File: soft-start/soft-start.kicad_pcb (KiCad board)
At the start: 2 copper layers, 26 parts, among them Q1 IRFB3004PbF, U1 4011, U2 CD4060BE

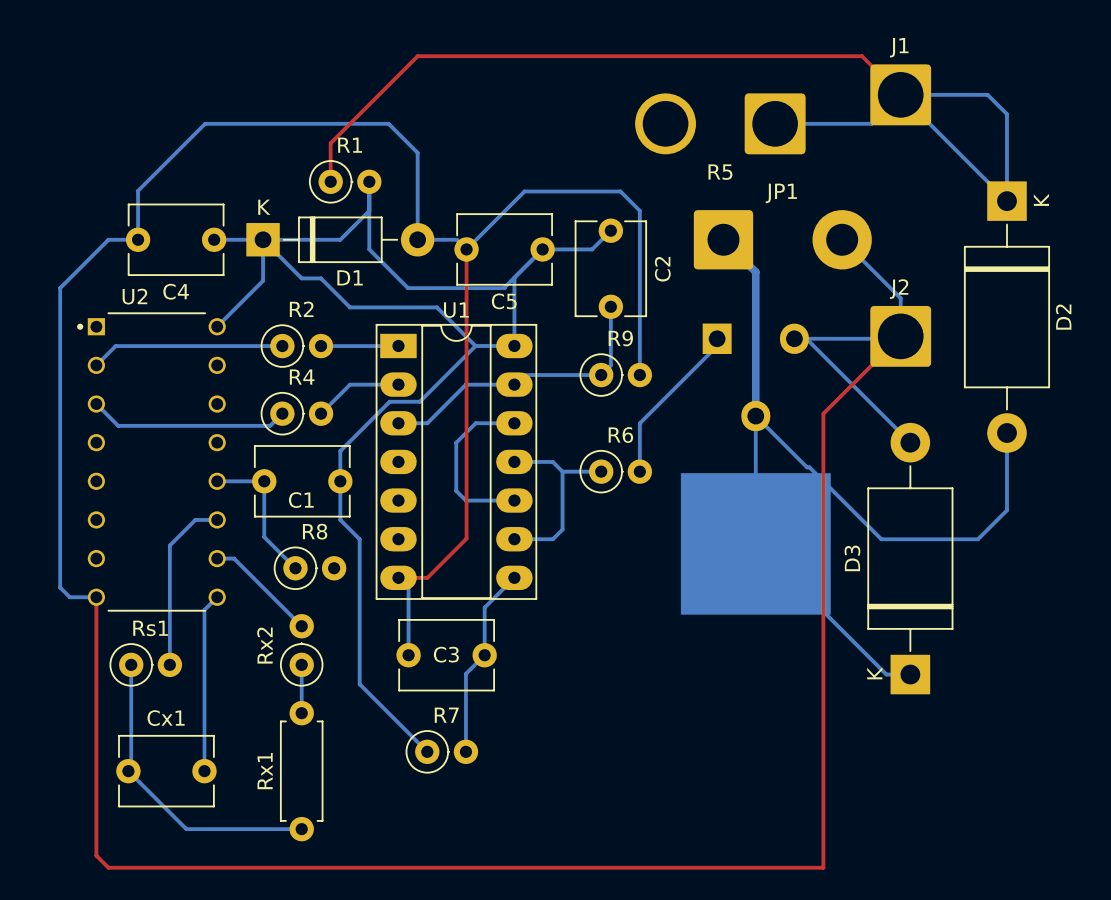
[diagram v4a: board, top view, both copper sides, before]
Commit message: [soft-start] Update schematic and add PCB
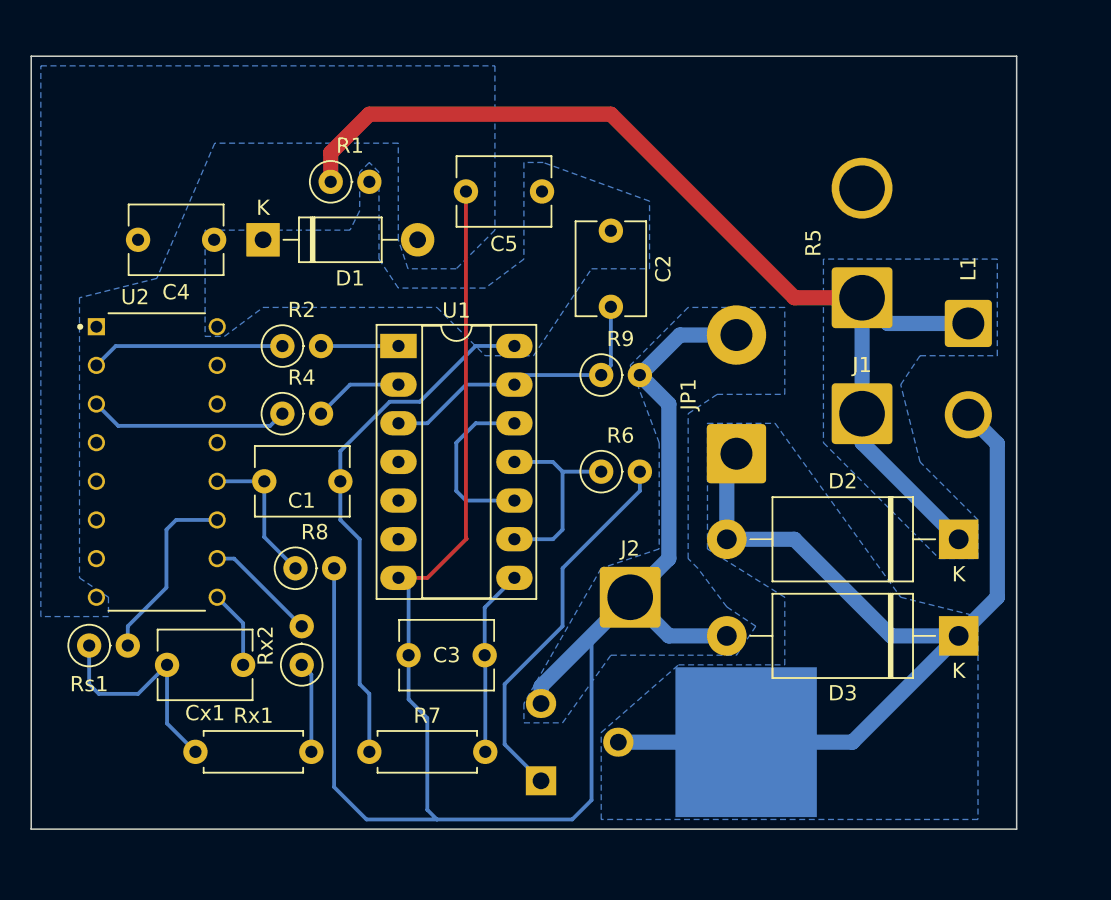
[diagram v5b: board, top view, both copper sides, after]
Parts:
- added L1: 12V Relay, Connector_Wire:SolderWire-1.5sqmm_1x02_P6mm_D1.7mm_OD3mm, F.Cu at (135.3, 103.9)
- R7: footprint Resistor_THT:R_Axial_DIN0207_L6.3mm_D2.5mm_P2.54mm_Vertical -> Resistor_THT:R_Axial_DIN0207_L6.3mm_D2.5mm_P7.62mm_Horizontal
- moved Q1 24.8 mm to (112.2, 134.0), turned to 90 degrees
- moved J2 24.7 mm to (113.0, 121.9)
- moved D2 22.5 mm to (134.6, 118.1), turned to 180 degrees
- moved J1 21.1 mm to (128.3, 109.9)
- moved JP1 14.1 mm to (120.0, 112.5), turned to 90 degrees
- moved R5 12.8 mm to (128.3, 102.2), turned to 90 degrees
- moved Rx1 8.64 mm to (84.5, 132.1), turned to 0 degrees
- moved Cx1 7.43 mm to (82.6, 126.4)
- moved D3 4.07 mm to (134.6, 124.5), turned to 180 degrees
- moved C5 3.81 mm to (107.2, 95.2)
- moved R7 3.81 mm to (95.9, 132.1)
- moved Rs1 3.04 mm to (77.5, 125.1)
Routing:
- net GND: track 244.8 -> 133.1 mm
- net VCC: track 103.2 -> 34.9 mm
- net Net-(Q1-G): track 10.8 -> 25.0 mm
- net Net-(U2-(PHI)O): track 11.8 -> 5.15 mm
- net +BATT: track 75.6 -> 69.1 mm
- net Net-(Cx1-Pad1): track 20.0 -> 15.2 mm
- net Net-(Rx1-Pad2): track 3.17 -> 5.98 mm
- net Net-(D2-A2): track 63.6 -> 65.4 mm
- net Net-(U2-(PHI)I): track 11.7 -> 12.3 mm
- added copper zone on B.Cu, net +BATT
- added copper zone on B.Cu, net GND
- added copper zone on B.Cu, net Net-(D2-A2)
- added copper zone on B.Cu, net VCC
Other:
- board outline added: 64.8 x 50.8 mm

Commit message: [soft-start] Update PCB - decrease dimensions, remove hard tracks.
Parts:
- removed C2: C, Capacitor_THT:C_Disc_D6.0mm_W4.4mm_P5.00mm
- removed R5: 0.18, 25W?, Connector_Wire:SolderWire-2.5sqmm_1x02_P7.2mm_D2.4mm_OD3.6mm
- C1, C3: value C -> 22nF
- R1, R2, R4: footprint Resistor_THT:R_Axial_DIN0207_L6.3mm_D2.5mm_P2.54mm_Vertical -> Resistor_THT:R_Axial_DIN0207_L6.3mm_D2.5mm_P7.62mm_Horizontal
- R7, R8, R9: value R -> 5.1k
- moved R1 30.5 mm to (123.8, 96.5), turned to 180 degrees
- moved R4 15.4 mm to (80.6, 97.8)
- moved J1 12.7 mm to (128.3, 97.2)
- moved D1 11.6 mm to (100.3, 96.5)
- moved R2 10.5 mm to (80.6, 101.0)
- moved C4 10.3 mm to (95.9, 99.6), turned to 90 degrees
- moved L1 7.64 mm to (127.6, 104.5)
- moved C5 6.50 mm to (108.6, 101.6), turned to 0 degrees
- moved Rs1 3.44 mm to (80.0, 127.4), turned to 90 degrees
- moved R9 0.76 mm to (111.5, 108.0), turned to 180 degrees
- moved R6 0.64 mm to (110.5, 113.7), turned to -90 degrees
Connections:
- R9 pad 1: /TRIGGER_SET -> VCC
- R9 pad 2: GND -> /TRIGGER_SET
- U1 pad 1: Net-(R2-Pad2) -> Net-(R4-Pad2)
- U1 pad 2: Net-(R4-Pad2) -> Net-(R2-Pad2)
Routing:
- net +BATT: track 69.1 -> 0.90 mm
- net Net-(D2-A2): track 65.4 -> 0.90 mm
- net GND: track 133.1 -> 160.2 mm
- net VCC: track 34.9 -> 61.8 mm
- net Net-(R2-Pad2): track 5.09 -> 12.4 mm
- net /TRIGGER_SET: track 19.4 -> 12.2 mm
- net Net-(R4-Pad2): track 5.88 -> 12.7 mm
- net Net-(Cx1-Pad1): track 15.2 -> 9.50 mm
- net Net-(U2-Q13): track 12.8 -> 7.67 mm
- net Net-(U2-Q14): track 13.2 -> 17.0 mm
- net Net-(Q1-G): track 25.0 -> 21.5 mm
- net /TRIGGER_OUT: track 13.2 -> 12.6 mm
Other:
- board size 64.8 x 50.8 mm -> 64.8 x 45.1 mm

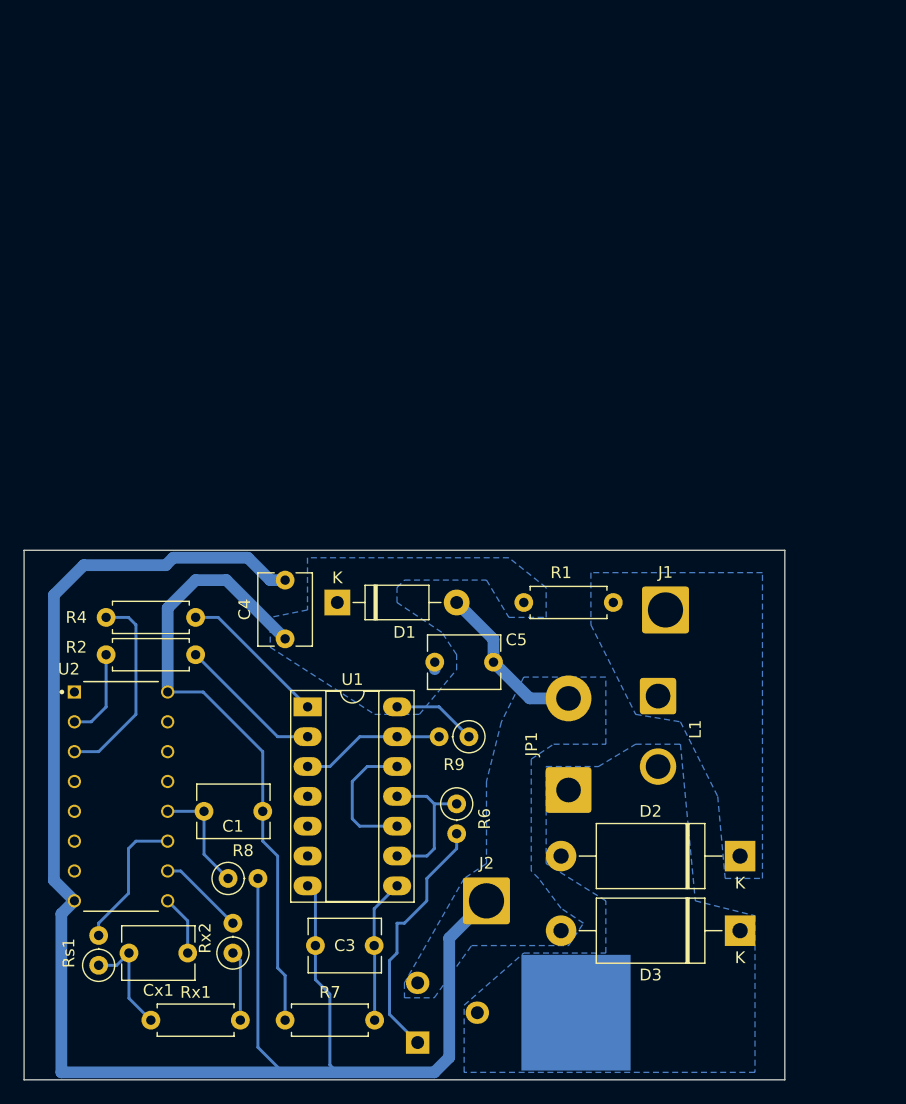
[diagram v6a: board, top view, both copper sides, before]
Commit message: [soft-start] Schematic - add fixes for trigger. Update PCB.
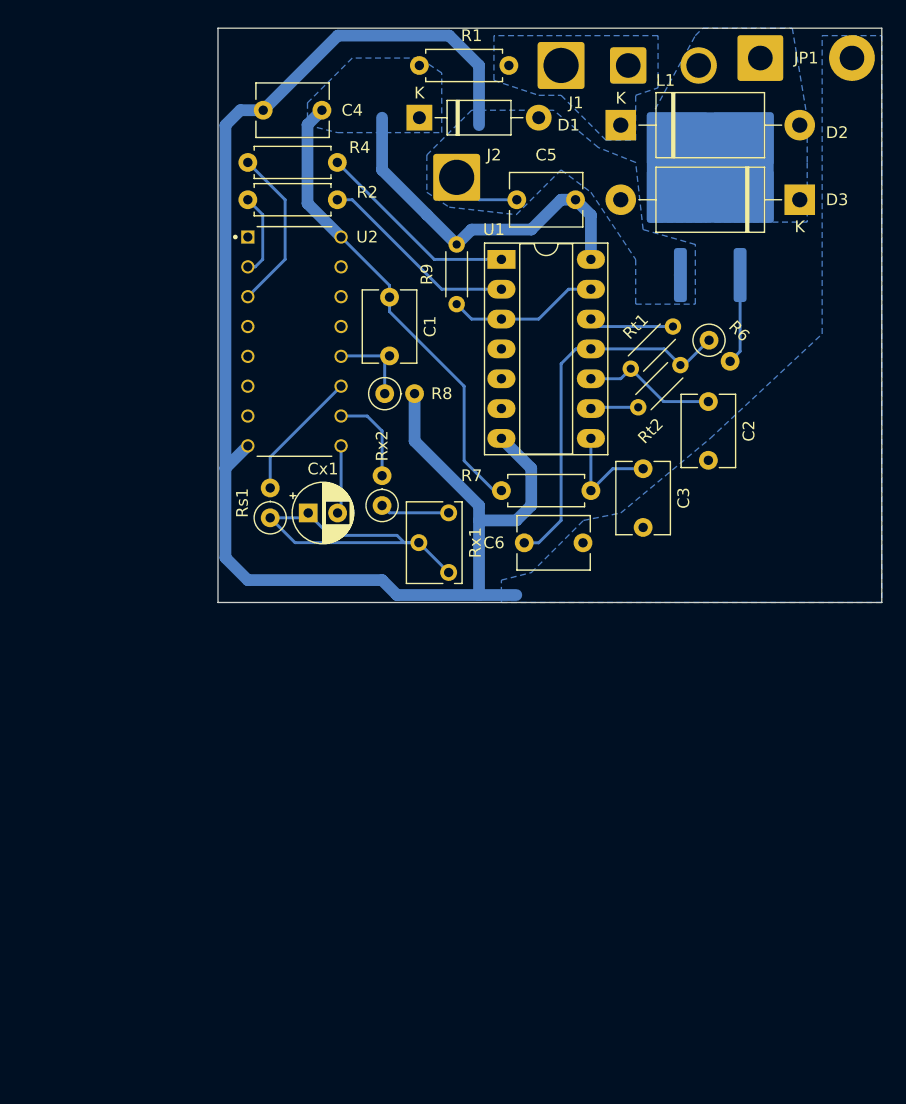
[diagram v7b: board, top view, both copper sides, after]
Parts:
- added C2: 22nF, Capacitor_THT:C_Disc_D6.0mm_W4.4mm_P5.00mm, F.Cu at (131.9, 79.4)
- added C6: 22nF, Capacitor_THT:C_Disc_D6.0mm_W4.4mm_P5.00mm, F.Cu at (116.2, 91.4)
- added Rt1: 5.1k, Resistor_THT:R_Axial_DIN0204_L3.6mm_D1.6mm_P5.08mm_Horizontal, F.Cu at (125.9, 79.9)
- added Rt2: 5.1k, Resistor_THT:R_Axial_DIN0204_L3.6mm_D1.6mm_P5.08mm_Horizontal, F.Cu at (128.9, 73.0)
- C4, C5: value C -> 0.1u
- Cx1: footprint Capacitor_THT:C_Disc_D6.0mm_W4.4mm_P5.00mm -> Capacitor_THT:CP_Radial_D5.0mm_P2.50mm
- Q1: footprint LIB:TO-220-3-4_Horizontal_TabDown -> Package_TO_SOT_SMD:TO-263-2
- R9: footprint Resistor_THT:R_Axial_DIN0207_L6.3mm_D2.5mm_P2.54mm_Vertical -> Resistor_THT:R_Axial_DIN0204_L3.6mm_D1.6mm_P5.08mm_Horizontal
- Rx1: value 6.8k -> 5k; footprint Resistor_THT:R_Axial_DIN0207_L6.3mm_D2.5mm_P7.62mm_Horizontal -> Potentiometer_THT:Potentiometer_Bourns_3266W_Vertical
- Rx2: value 3.3k -> 4.7k
- moved Q1 75.6 mm to (132.1, 61.0)
- moved JP1 64.4 mm to (136.3, 50.2), turned to 0 degrees
- moved D2 63.1 mm to (124.5, 55.9), turned to 0 degrees
- moved D3 62.4 mm to (139.7, 62.2)
- moved J2 61.6 mm to (110.5, 60.3)
- moved L1 53.8 mm to (125.1, 50.8), turned to 0 degrees
- moved R7 48.7 mm to (114.3, 87.0)
- moved J1 47.2 mm to (119.4, 50.8)
- moved C3 46.6 mm to (126.4, 85.1), turned to -90 degrees
- moved R1 46.6 mm to (114.9, 50.8)
- moved Rx1 45.8 mm to (109.8, 94.0), turned to -90 degrees
- moved C4 45.1 mm to (99.0, 54.6), turned to 180 degrees
- moved C1 45.1 mm to (104.8, 70.5), turned to -90 degrees
- moved R6 44.9 mm to (132.0, 74.2), turned to -45 degrees
- moved R8 43.4 mm to (104.4, 78.7)
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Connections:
- Rx1 pad 2: Net-(Rx1-Pad2) -> Net-(Cx1-Pad1)
- Rx2 pad 1: Net-(Rx1-Pad2) -> Net-(Rx1-Pad3)
- U1 pad 10: Net-(U1-Pad10) -> Net-(C2-Pad1)
- U1 pad 12: Net-(U1-Pad10) -> Net-(Rt2-Pad1)
- U1 pad 9: /TRIGGER_OUT -> Net-(Rt1-Pad1)
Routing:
- net GND: track 160.2 -> 134.8 mm
- net Net-(Cx1-Pad1): track 9.50 -> 31.0 mm
- net /TRIGGER_OUT: track 12.6 -> 31.8 mm
- net Net-(D2-A2): track 0.90 -> 14.9 mm
- net Net-(Q1-G): track 21.5 -> 7.70 mm
- net Net-(U1-Pad10): track 11.6 -> 0.00 mm
- net Net-(C2-Pad1): track 0.00 -> 11.5 mm
- net VCC: track 61.8 -> 72.4 mm
- net Net-(Rt2-Pad1): track 0.00 -> 7.25 mm
- net Net-(Rx1-Pad2): track 5.98 -> 0.00 mm
- net Net-(Rx1-Pad3): track 0.00 -> 5.93 mm
- net Net-(R4-Pad2): track 12.7 -> 17.4 mm
- net Net-(R2-Pad2): track 12.4 -> 17.1 mm
- net Net-(Rt1-Pad1): track 0.00 -> 4.07 mm
- net Net-(U2-Q14): track 17.0 -> 14.1 mm
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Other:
- board size 64.8 x 45.1 mm -> 56.5 x 48.9 mm

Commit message: [soft-start] Update values of timing RC
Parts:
- removed R6: 100 .. 1k, Resistor_THT:R_Axial_DIN0207_L6.3mm_D2.5mm_P2.54mm_Vertical
- moved C6 19.1 mm to (131.5, 80.0)
- moved C2 5.77 mm to (131.5, 73.7), turned to 0 degrees
- moved Rt2 0.64 mm to (128.9, 72.4), turned to -90 degrees
- moved Rt1 0.43 mm to (126.4, 80.0), turned to 90 degrees
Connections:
- Q1 pad 1: Net-(Q1-G) -> /TRIGGER_OUT
- Rt1 pad 1: Net-(Rt1-Pad1) -> /TRIGGER_OUT
- Rt1 pad 2: /TRIGGER_OUT -> Net-(Rt1-Pad2)
- Rt2 pad 1: Net-(Rt2-Pad1) -> Net-(C2-Pad1)
- Rt2 pad 2: Net-(C2-Pad1) -> Net-(Rt2-Pad2)
- U1 pad 10: Net-(C2-Pad1) -> Net-(Rt2-Pad2)
- U1 pad 11: /TRIGGER_OUT -> Net-(Rt1-Pad2)
- U1 pad 12: Net-(Rt2-Pad1) -> Net-(C2-Pad1)
- U1 pad 9: Net-(Rt1-Pad1) -> /TRIGGER_OUT
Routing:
- net /TRIGGER_OUT: track 31.8 -> 22.3 mm
- net Net-(Q1-G): track 7.70 -> 0.00 mm
- net Net-(Rt2-Pad1): track 7.25 -> 0.00 mm
- net Net-(Rt2-Pad2): track 0.00 -> 6.98 mm
- net GND: track 134.8 -> 140.5 mm
- net Net-(Rt1-Pad2): track 0.00 -> 4.44 mm
- net Net-(Rt1-Pad1): track 4.07 -> 0.00 mm
- net Net-(C2-Pad1): track 11.5 -> 10.1 mm
